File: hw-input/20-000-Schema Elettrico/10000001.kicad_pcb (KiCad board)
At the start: 4 copper layers, 45.7 x 32 mm, 35 parts, among them IC1 TLP291, IC2 TLP291, P1 CONN_4, P2 CONN_4, P3 CONN_4, P4 CONN_4, P5 CONN_4, P6 CONN_4, P7 CONN_4, P8 CONN_4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

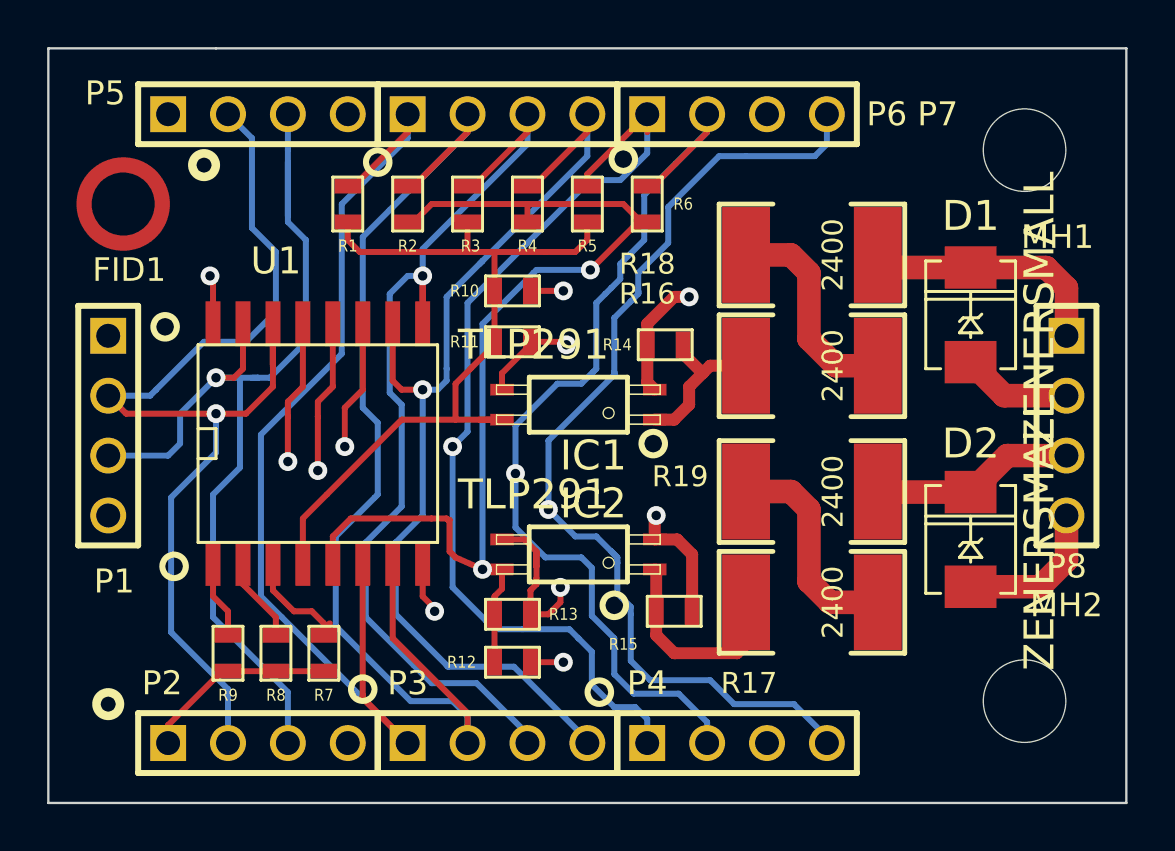
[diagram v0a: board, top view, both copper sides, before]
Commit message: Aggiunte capacità di bypass su alimentazione I2C expander
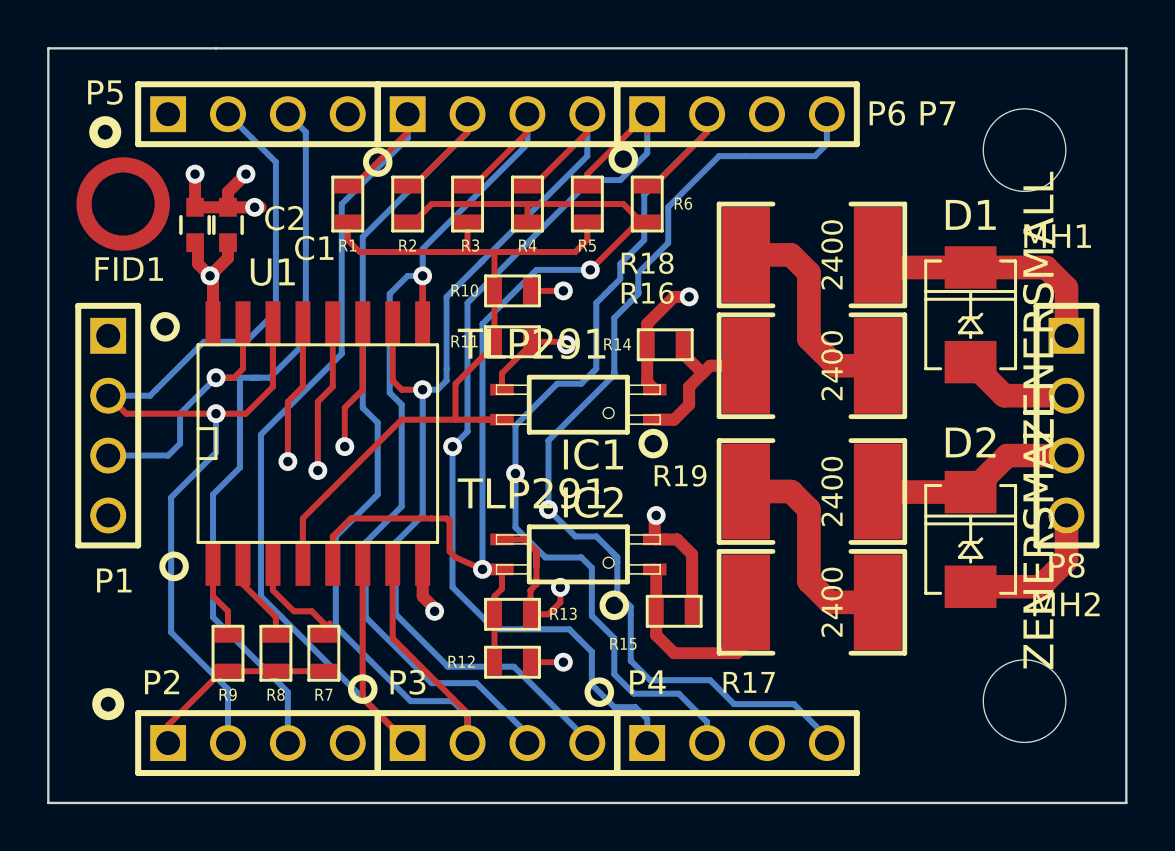
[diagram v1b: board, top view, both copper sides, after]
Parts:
- added C1: 100n, Capacitors_SMD:C_0603, F.Cu at (91.4, 50.4)
- added C2: 1u, Capacitors_SMD:C_0603, F.Cu at (90.0, 50.4)
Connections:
- P4 pad 3: (no net) -> Net-(P4-Pad3)
- P7 pad 3: (no net) -> Net-(P7-Pad3)
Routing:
- net GND: track 13.5 -> 19.7 mm, vias 3 -> 6
- net VDD: track 13.2 -> 16.6 mm
- net /I2C_SDA: track 44.1 -> 41.8 mm
